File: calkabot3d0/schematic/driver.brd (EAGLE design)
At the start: 65 x 50 mm, 48 parts

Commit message: teraz schemat wygląda ładnie
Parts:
- removed SDA: (no value), pinhead:1X02
- added C15: (no value), rcl:C0603
- moved R14 17.0 mm to (13.5, 11.5), flipped to the bottom, turned to 180 degrees
- moved C12 2.00 mm to (17.4, 47.3)
- moved 12V 0.50 mm to (40.5, 20.0)
- moved R4 0.50 mm to (44.5, 20.0)
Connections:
- new net N$13: C15.1, STM32.1
- net GND: now also C15.2
- net SCL: no longer SDA.1
- net SDA: no longer SDA.2
- net VCC: no longer R14.2
- net VDD: now also R14.2; no longer STM32.1
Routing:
- net GND: track 396.0 -> 383.7 mm, vias 8 -> 9
- net VDD: track 214.3 -> 204.1 mm
- net NRST: track 77.6 -> 85.6 mm
- net N$4: track 14.4 -> 8.76 mm
- net SCL: track 18.3 -> 15.6 mm
- net N$13: track 0.00 -> 2.67 mm
- net VBUS: track 45.5 -> 43.5 mm
- net SDA: track 17.6 -> 15.9 mm
- net 12V: track 13.1 -> 12.4 mm

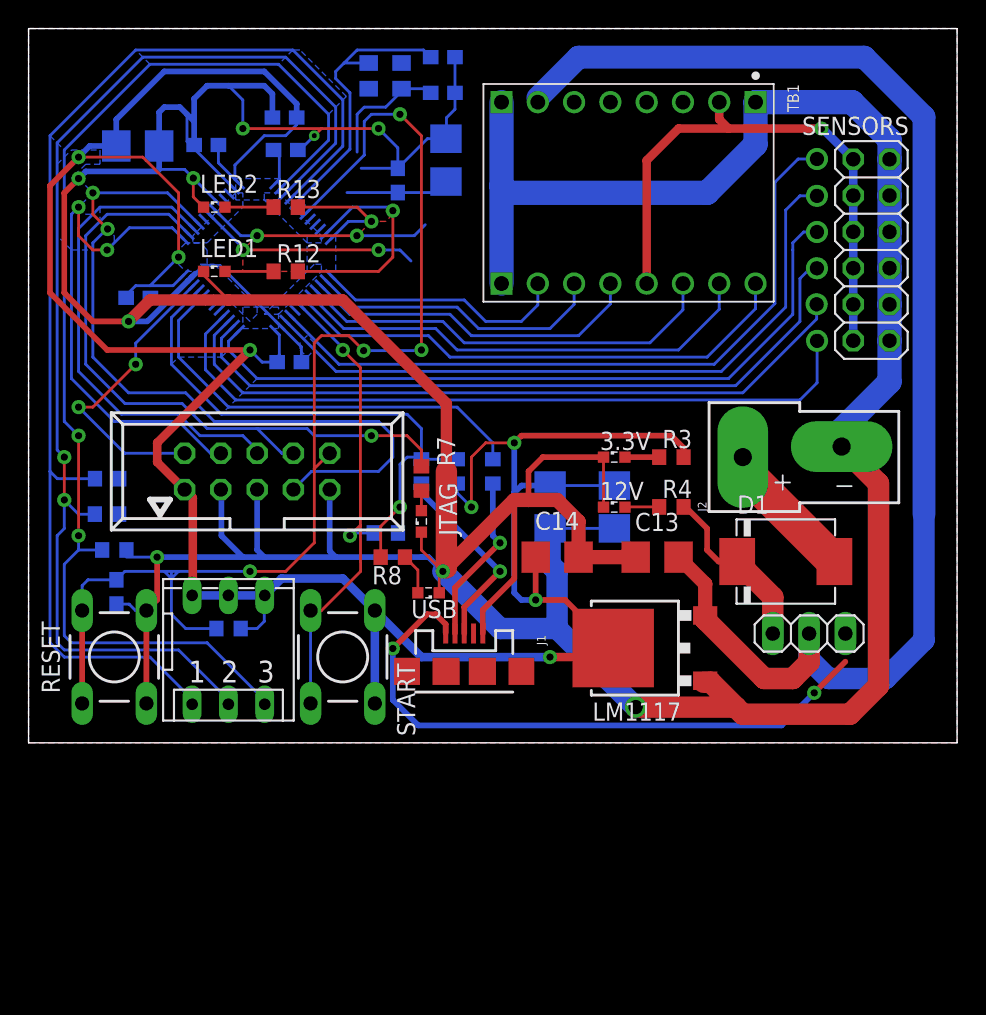
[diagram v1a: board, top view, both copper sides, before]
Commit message: Jtag ssie, zrobiłem SWD. Zmiana płyki. pomniejszenie dodanie resetu itd.
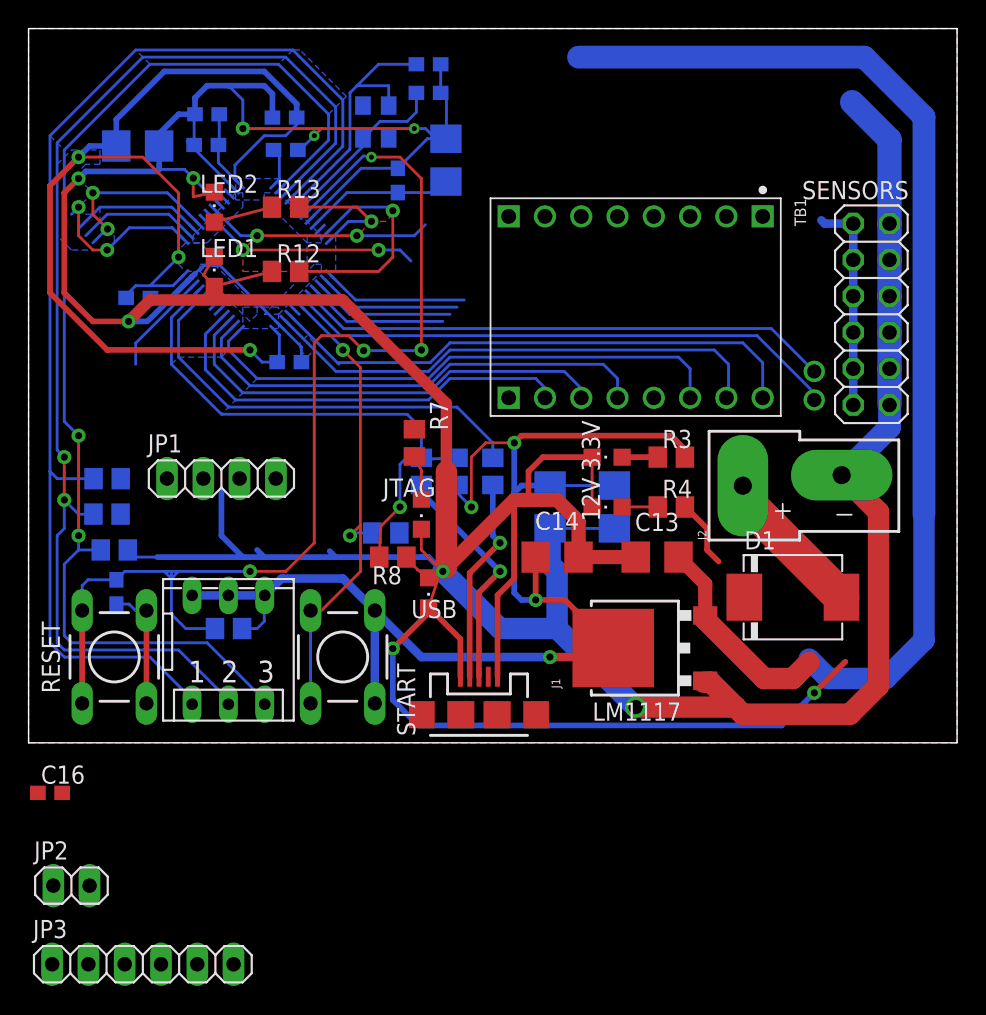
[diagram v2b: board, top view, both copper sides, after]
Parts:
- removed TCLK: 057-010-1, con-panduit:057-010-1
- added C16: 4,7u, rcl:C0603
- added C17: 100n, rcl:C0603
- added JP1: (no value), pinhead:1X04
- added JP2: (no value), pinhead:1X02
- 12V, 3.3V, JTAG, LED1, LED2, USB: device led:SML0603 -> led:CHIPLED_0805
- C15, C9: value (none) -> 100n
- JP3: device pinhead:1X03 -> pinhead:1X06
- R1, R12, R13, R14, R2, R3, R4, R5, R6, R7, R8, R9: device rcl:R0603 -> rcl:R0805
- R10: value 1k -> 10; device rcl:R0603 -> rcl:R0805
- R11: value 1k5 -> 10k; device rcl:R0603 -> rcl:R0805
- moved JP3 52.1 mm to (7.50, -12.0), turned to 0 degrees
- moved TB1 8.02 mm to (42.0, 34.0)
- moved SENSORS 4.50 mm to (58.5, 33.5)
- moved Q1 3.29 mm to (23.8, 47.0), turned to 270 degrees
- moved J1 3.20 mm to (31.0, 5.47)
- moved D1 2.55 mm to (53.0, 13.7)
- moved R7 2.55 mm to (26.5, 24.5)
- moved J2 2.00 mm to (49.5, 21.5)
- moved C11 1.12 mm to (27.5, 51.0)
- moved C10 1.00 mm to (27.5, 49.0)
- moved 12V 0.50 mm to (40.0, 20.0), turned to 90 degrees
- moved 3.3V 0.50 mm to (40.0, 23.5), turned to 90 degrees
- moved JTAG 0.50 mm to (27.0, 19.5), turned to 180 degrees
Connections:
- removed net 12V: D1.C, JP3.3, R4.2
- removed net TCLK: STM32.37, TCLK.4
- removed net TMS: STM32.34, TCLK.2
- removed net VBUS: J1.VBUS, JP3.1
- new net N$14: JP2.1
- new net SWCLK: JP1.2, R7.2, STM32.37
- new net SWDIO: JP1.4, STM32.34
- net GND: now also C16.2, C17.2, JP1.3; no longer TCLK.3, TCLK.5, TCLK.9
- net MA1: now also STM32.25; no longer STM32.16
- net MA2: now also STM32.22; no longer STM32.17
- net MB1: now also STM32.26; no longer STM32.15
- net MB2: now also STM32.27; no longer STM32.14
- net N$13: now also JP2.2; no longer C15.1, STM32.1
- net N$3: now also Q1.1; no longer Q1.3
- net N$4: now also Q1.3; no longer Q1.1
- net NRST: no longer TCLK.10
- net PWMA: now also STM32.21; no longer STM32.18
- net PWMB: now also STM32.28; no longer STM32.13
- net S0: now also JP3.1, STM32.18; no longer STM32.21
- net S1: now also JP3.2, STM32.17; no longer STM32.22
- net S2: now also JP3.3, STM32.16; no longer STM32.25
- net S3: now also JP3.4, STM32.15; no longer STM32.26
- net S4: now also JP3.5, STM32.14; no longer STM32.27
- net S5: now also JP3.6, STM32.13; no longer STM32.28
- net STAB: now also D1.C, R4.2; no longer JP3.2
- net TDI: no longer R7.2, TCLK.8
- net TDO: no longer TCLK.6
- net TRST: no longer TCLK.7
- net VDD: now also C15.1, C16.1, C17.1, J1.VBUS, JP1.1, STM32.1; no longer TCLK.1
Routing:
- net GND: track 383.7 -> 326.2 mm, vias 9 -> 8
- net VBUS: track 43.5 -> 0.00 mm, vias 2 -> 0
- net S5: track 51.5 -> 10.1 mm, vias 1 -> 0
- net S2: track 50.9 -> 9.85 mm, vias 1 -> 0
- net TRST: track 53.4 -> 12.7 mm
- net S3: track 50.3 -> 9.93 mm, vias 1 -> 0
- net S4: track 49.7 -> 10.0 mm, vias 1 -> 0
- net TDI: track 47.8 -> 8.43 mm, vias 1 -> 0
- net TCLK: track 35.6 -> 0.00 mm, vias 2 -> 0
- net VDD: track 204.1 -> 237.9 mm, vias 7 -> 9
- net TDO: track 34.4 -> 9.35 mm
- net VCC: track 39.7 -> 15.0 mm, vias 1 -> 0
- net TMS: track 21.2 -> 0.00 mm, vias 2 -> 0
- net PWMB: track 17.9 -> 30.6 mm
- net 12V: track 12.4 -> 0.00 mm
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
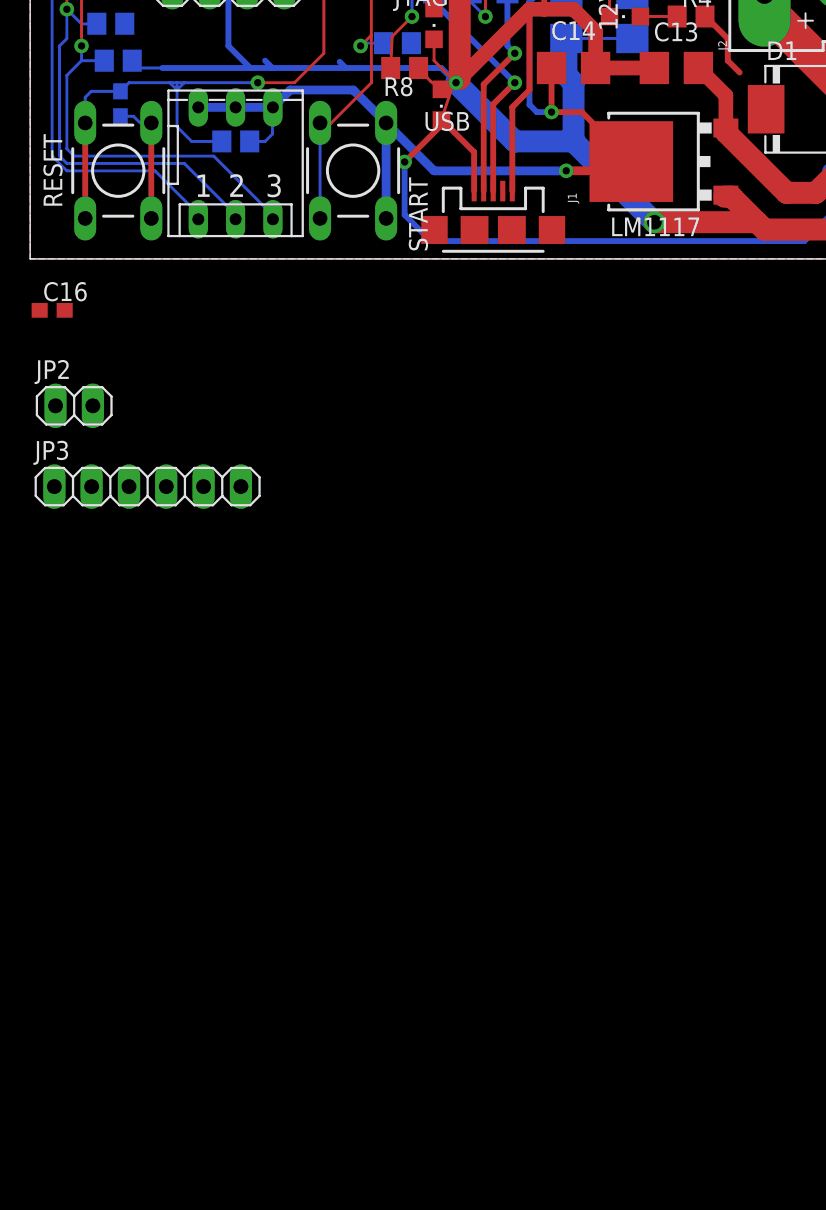
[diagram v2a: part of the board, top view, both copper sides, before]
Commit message: Adding I2C pull-up resistors, 5V on board, change package for LM1117, PB2 (BOOT1) short to GND
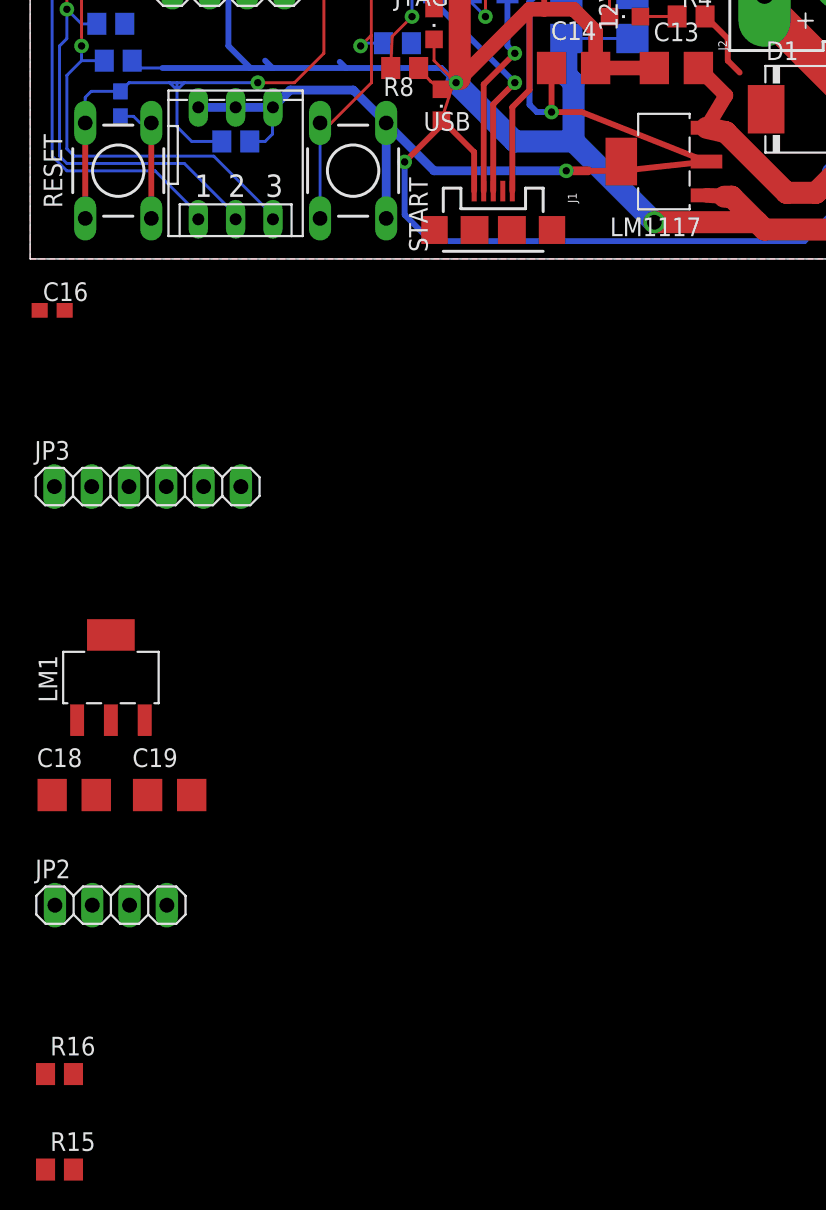
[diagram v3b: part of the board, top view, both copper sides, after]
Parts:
- added C18, C19: 10u, rcl:CT3528
- added LM1: LM1117MP-3.3, lm1117_11:SOT223
- added R15, R16: 4k7, rcl:R0805
- JP2: device pinhead:1X02 -> pinhead:1X04
- LM1117: value LM1117DT-3.3 -> LM1117MP-3.3; device lm1117_10:TO252 -> lm1117_11:SOT223
- R10: value 10 -> 10k
- moved JP2 34.1 mm to (5.00, -40.5)
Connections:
- removed net N$13: JP2.2
- removed net N$14: JP2.1
- new net SWDA: JP1.2
- net GND: now also C18.-, C19.-, JP1.4, JP2.3, LM1.1, STM32.20; no longer JP1.3
- net SCL: now also JP2.2, R16.1
- net SDA: now also JP2.1, R15.1
- net STAB: now also C18.+, LM1.3, LM1117.3; no longer LM1117.2
- net SWCLK: now also JP1.3; no longer JP1.2
- net SWDIO: no longer JP1.4
- net VCC: now also C19.+, JP2.4, LM1.2, LM1.4, R15.2, R16.2
- net VDD: now also LM1117.2, LM1117.4; no longer LM1117.3
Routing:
- net VDD: track 237.9 -> 247.2 mm
- net STAB: track 91.8 -> 93.2 mm
- net GND: track 326.2 -> 327.3 mm

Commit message: Adding motor outputs
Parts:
- removed JP3: (no value), pinhead:1X06
- removed SENSORS: (no value), pinhead:2X06
- added JP4, JP5: (no value), pinhead:1X02/90
- moved LED2 119.9 mm to (2.50, -78.5)
- moved LED1 108.5 mm to (11.5, -72.0)
- moved R13 106.5 mm to (7.00, -65.0)
- moved R12 102.8 mm to (1.50, -65.0)
- moved JTAG 100.0 mm to (7.00, -78.5), turned to 0 degrees
- moved R7 99.2 mm to (1.50, -71.5), turned to 0 degrees
- moved USB 92.9 mm to (11.5, -77.5), turned to 0 degrees
- moved R8 90.0 mm to (6.00, -71.5), turned to 0 degrees
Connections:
- net GND: no longer SENSORS.1, SENSORS.11, SENSORS.3, SENSORS.5, SENSORS.7, SENSORS.9
- net N$42: now also JP4.2
- net N$43: now also JP4.1
- net N$44: now also JP5.2
- net N$45: now also JP5.1
- net S0: no longer JP3.1
- net S1: no longer JP3.2
- net S2: no longer JP3.3
- net S3: no longer JP3.4
- net S4: no longer JP3.5
- net S5: no longer JP3.6
- net VCC: no longer SENSORS.10, SENSORS.12, SENSORS.2, SENSORS.4, SENSORS.6, SENSORS.8
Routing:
- net GND: track 327.3 -> 288.2 mm
- net NRST: track 78.4 -> 62.3 mm
- net VCC: track 15.0 -> 0.00 mm
- net LED1: track 15.8 -> 10.3 mm
- net N$8: track 4.18 -> 0.00 mm
- net N$5: track 4.18 -> 0.00 mm
- net LED2: track 8.86 -> 4.81 mm
- net N$10: track 3.16 -> 0.00 mm
- net D+: track 38.8 -> 36.6 mm
- net N$11: track 2.13 -> 0.00 mm
- net BAT+: track 10.7 -> 9.77 mm

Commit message: Change board
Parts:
- removed JP1, JP2: (no value), pinhead:1X04
- added I2C, SWD: (no value), pinhead:1X04
- moved USB 155.3 mm to (-29.2, 72.4)
- moved JTAG 147.9 mm to (-24.1, 66.0)
- moved LED2 146.1 mm to (-19.1, 66.0)
- moved LED1 140.4 mm to (-14.0, 66.0)
- moved R8 137.6 mm to (-35.6, 59.7)
- moved R7 135.0 mm to (-30.5, 59.7)
- moved JP5 133.5 mm to (47.0, 43.2)
- moved JP4 126.6 mm to (40.6, 43.2)
- moved R13 123.8 mm to (-29.2, 53.3)
- moved R12 120.8 mm to (-22.9, 53.3)
- moved R15 120.0 mm to (-41.9, 53.3)
- moved R16 116.5 mm to (-48.3, 53.3)
- moved C8 112.5 mm to (-64.8, 59.7), flipped to the top, turned to 0 degrees
- moved R4 108.2 mm to (-58.4, 53.3)
- moved C19 105.2 mm to (-63.5, 43.2)
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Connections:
- net GND: now also I2C.3, SWD.4; no longer JP1.4, JP2.3
- net SCL: now also I2C.2; no longer JP2.2
- net SDA: now also I2C.1; no longer JP2.1
- net SWCLK: now also SWD.3; no longer JP1.3
- net SWDA: now also SWD.2; no longer JP1.2
- net VCC: now also I2C.4; no longer JP2.4
- net VDD: now also SWD.1; no longer JP1.1
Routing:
- net GND: track 288.2 -> 36.9 mm, vias 8 -> 0
- net VDD: track 247.2 -> 12.9 mm, vias 9 -> 1
- net PC15: track 83.6 -> 0.00 mm
- net PC14: track 83.0 -> 0.00 mm, vias 2 -> 0
- net PC13: track 81.6 -> 0.00 mm, vias 2 -> 0
- net NRST: track 62.3 -> 0.00 mm, vias 4 -> 0
- net STAB: track 93.2 -> 48.8 mm, vias 0 -> 1
- net S0: track 38.8 -> 0.00 mm, vias 1 -> 0
- net PWMA: track 38.2 -> 0.00 mm
- net MA1: track 37.8 -> 0.00 mm
- net S1: track 37.5 -> 0.00 mm, vias 1 -> 0
- net D+: track 36.6 -> 0.00 mm, vias 1 -> 0
- net MA2: track 36.0 -> 0.00 mm
- net BUT: track 34.2 -> 0.00 mm, vias 2 -> 0
- net MB1: track 33.5 -> 0.00 mm
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- removed copper zone on layer 16, net N$12
- removed copper zone on layer 16, net N$15
- removed copper zone on layer 1, net N$16
- removed copper zone on layer 16, net N$22
- removed copper zone on layer 16, net N$24
- removed copper zone on layer 16, net N$25
- removed copper zone on layer 16, net N$26
- removed copper zone on layer 16, net N$27
- removed copper zone on layer 16, net N$28
- removed copper zone on layer 16, net N$29
- removed copper zone on layer 16, net N$30
- removed copper zone on layer 16, net N$31
- removed copper zone on layer 16, net N$32
- removed copper zone on layer 16, net N$33
- removed copper zone on layer 1, net N$39
- removed copper zone on layer 16, net N$9
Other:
- board size 65 x 50 mm -> 60.9 x 42.9 mm
